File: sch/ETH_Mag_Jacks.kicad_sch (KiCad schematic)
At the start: 3 parts, among them J1 0826-1X4T-HS-F, J2 0826-1X4T-HS-F

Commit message: Project recovered
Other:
- company: (none) -> Karlsruhe Institute of Technology (KIT)
- title: (none) -> ATCA Simple Loopback HUB
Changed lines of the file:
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@@
 (kicad_sch (version 20230121) (generator eeschema)
   (paper "A4")
+  (title_block
+    (title "ATCA Simple Loopback HUB")
+    (date "2023-09-12")
+    (rev "1.0")
+    (company "Karlsruhe Institute of Technology (KIT)")
+    (comment 1 "Institute for Data Processing and Electronics (IPE)")
+    (comment 2 "Luis Ardila")
+    (comment 3 "IPE-380-06")
+    (comment 4 "Licensed under CERN-OHL-P-2.0")
+  )
   (no_connect (at 241.3 72.39))
   (no_connect (at 241.3 124.46))
@@
     (pin "9_4")
     (instances
-      (project "atca_simple_hub"
+      (project "atca-simple-loopback-hub"
         (path "/b1bf14e0-f6d2-45a7-b67f-6500a354b7ad/721cf5b7-470b-44a1-8f61-80b0cd462786"
           (reference "J1") (unit 1)
@@
     (pin "9_4")
     (instances
-      (project "atca_simple_hub"
+      (project "atca-simple-loopback-hub"
         (path "/b1bf14e0-f6d2-45a7-b67f-6500a354b7ad/721cf5b7-470b-44a1-8f61-80b0cd462786"
           (reference "J1") (unit 1)
@@
     (pin "9_4")
     (instances
-      (project "atca_simple_hub"
+      (project "atca-simple-loopback-hub"
         (path "/b1bf14e0-f6d2-45a7-b67f-6500a354b7ad/9c66bb85-f11b-42a4-b8f0-ea5e834ff554"
           (reference "J2") (unit 3)
@@
     (pin "9_4")
     (instances
-      (project "atca_simple_hub"
+      (project "atca-simple-loopback-hub"
         (path "/b1bf14e0-f6d2-45a7-b67f-6500a354b7ad/9c66bb85-f11b-42a4-b8f0-ea5e834ff554"
           (reference "J1") (unit 4)
@@
     (pin "9_4")
     (instances
-      (project "atca_simple_hub"
+      (project "atca-simple-loopback-hub"
         (path "/b1bf14e0-f6d2-45a7-b67f-6500a354b7ad/9c66bb85-f11b-42a4-b8f0-ea5e834ff554"
           (reference "J2") (unit 4)
@@
     (pin "9_4")
     (instances
-      (project "atca_simple_hub"
+      (project "atca-simple-loopback-hub"
         (path "/b1bf14e0-f6d2-45a7-b67f-6500a354b7ad/9c66bb85-f11b-42a4-b8f0-ea5e834ff554"
           (reference "J1") (unit 3)
@@
     (pin "9_4")
     (instances
-      (project "atca_simple_hub"
+      (project "atca-simple-loopback-hub"
         (path "/b1bf14e0-f6d2-45a7-b67f-6500a354b7ad/721cf5b7-470b-44a1-8f61-80b0cd462786"
           (reference "J1") (unit 2)
@@
     (pin "9_4")
     (instances
-      (project "atca_simple_hub"
+      (project "atca-simple-loopback-hub"
         (path "/b1bf14e0-f6d2-45a7-b67f-6500a354b7ad/721cf5b7-470b-44a1-8f61-80b0cd462786"
           (reference "J1") (unit 2)

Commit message: sch work
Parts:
- added C45 (x8), C47 (x8), C49 (x8), C59 (x8): 100nF, Capacitor_SMD:C_0402_1005Metric, symbol Device:C
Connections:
- net Z2_BI1.A_N: now also J1.10_1 (TRD1-_1)
- net Z2_BI1.A_P: now also J1.11_1 (TRD1+_1)
- net Z2_BI1.B_N: now also J1.5_1 (TRD2-_1)
- net Z2_BI1.B_P: now also J1.4_1 (TRD2+_1)
- net Z2_BI1.C_N: now also J1.2_1 (TRD3-_1)
- net Z2_BI1.C_P: now also J1.3_1 (TRD3+_1)
- net Z2_BI1.D_N: now also J1.9_1 (TRD4-_1)
- net Z2_BI1.D_P: now also J1.8_1 (TRD4+_1)
- net Z2_BI2.A_N: now also J1.10_2 (TRD1-_2)
- net Z2_BI2.A_P: now also J1.11_2 (TRD1+_2)
- net Z2_BI2.B_N: now also J1.5_2 (TRD2-_2)
- net Z2_BI2.B_P: now also J1.4_2 (TRD2+_2)
- net Z2_BI2.C_N: now also J1.2_2 (TRD3-_2)
- net Z2_BI2.C_P: now also J1.3_2 (TRD3+_2)
- net Z2_BI2.D_N: now also J1.9_2 (TRD4-_2)
- net Z2_BI2.D_P: now also J1.8_2 (TRD4+_2)
- net Z2_BI3.A_N: now also J1.10_4 (TRD1-_4)
- net Z2_BI3.A_P: now also J1.11_4 (TRD1+_4)
- net Z2_BI3.B_N: now also J1.5_4 (TRD2-_4)
- net Z2_BI3.B_P: now also J1.4_4 (TRD2+_4)
- net Z2_BI3.C_N: now also J1.2_4 (TRD3-_4)
- net Z2_BI3.C_P: now also J1.3_4 (TRD3+_4)
- net Z2_BI3.D_N: now also J1.9_4 (TRD4-_4)
- net Z2_BI3.D_P: now also J1.8_4 (TRD4+_4)
- net Z2_BI4.A_N: now also J1.10_3 (TRD1-_3)
- net Z2_BI4.A_P: now also J1.11_3 (TRD1+_3)
- net Z2_BI4.B_N: now also J1.5_3 (TRD2-_3)
- net Z2_BI4.B_P: now also J1.4_3 (TRD2+_3)
- net Z2_BI4.C_N: now also J1.2_3 (TRD3-_3)
- net Z2_BI4.C_P: now also J1.3_3 (TRD3+_3)
- net Z2_BI4.D_N: now also J1.9_3 (TRD4-_3)
- net Z2_BI4.D_P: now also J1.8_3 (TRD4+_3)
- net Z2_BI5.A_N: now also J1.10_1 (TRD1-_1)
- net Z2_BI5.A_P: now also J1.11_1 (TRD1+_1)
- net Z2_BI5.B_N: now also J1.5_1 (TRD2-_1)
- net Z2_BI5.B_P: now also J1.4_1 (TRD2+_1)
- net Z2_BI5.C_N: now also J1.2_1 (TRD3-_1)
- net Z2_BI5.C_P: now also J1.3_1 (TRD3+_1)
- net Z2_BI5.D_N: now also J1.9_1 (TRD4-_1)
- net Z2_BI5.D_P: now also J1.8_1 (TRD4+_1)
- net Z2_BI6.A_N: now also J1.10_2 (TRD1-_2)
- net Z2_BI6.A_P: now also J1.11_2 (TRD1+_2)
- net Z2_BI6.B_N: now also J1.5_2 (TRD2-_2)
- net Z2_BI6.B_P: now also J1.4_2 (TRD2+_2)
- net Z2_BI6.C_N: now also J1.2_2 (TRD3-_2)
- net Z2_BI6.C_P: now also J1.3_2 (TRD3+_2)
- net Z2_BI6.D_N: now also J1.9_2 (TRD4-_2)
- net Z2_BI6.D_P: now also J1.8_2 (TRD4+_2)
- net Z2_BI7.A_N: now also J2.10_4 (TRD1-_4)
- net Z2_BI7.A_P: now also J2.11_4 (TRD1+_4)
- net Z2_BI7.B_N: now also J2.5_4 (TRD2-_4)
- net Z2_BI7.B_P: now also J2.4_4 (TRD2+_4)
- net Z2_BI7.C_N: now also J2.2_4 (TRD3-_4)
- net Z2_BI7.C_P: now also J2.3_4 (TRD3+_4)
- net Z2_BI7.D_N: now also J2.9_4 (TRD4-_4)
- net Z2_BI7.D_P: now also J2.8_4 (TRD4+_4)
- net Z2_BI8.A_N: now also J2.10_3 (TRD1-_3)
- net Z2_BI8.A_P: now also J2.11_3 (TRD1+_3)
- net Z2_BI8.B_N: now also J2.5_3 (TRD2-_3)
- net Z2_BI8.B_P: now also J2.4_3 (TRD2+_3)
- net Z2_BI8.C_N: now also J2.2_3 (TRD3-_3)
- net Z2_BI8.C_P: now also J2.3_3 (TRD3+_3)
- net Z2_BI8.D_N: now also J2.9_3 (TRD4-_3)
- net Z2_BI8.D_P: now also J2.8_3 (TRD4+_3)
- net at J1.12_1 (TRCT1_1): now also C45.1 (x2)
- net at J1.1_1 (TRCT3_1): now also C49.1 (x2)
- net at J1.6_1 (TRCT2_1): now also C47.1 (x2)
- net at J1.7_1 (TRCT4_1): now also C59.1 (x2)
- net GNDPWR: now reaches J1.S1 (SHIELD), J1.S2 (SHIELD)
- net GNDPWR: now also J1.S1 (SHIELD), J1.S2 (SHIELD)
- net at J2.12_3 (TRCT1_3): now also C45.1
- net at J2.1_3 (TRCT3_3): now also C49.1
- net at J2.6_3 (TRCT2_3): now also C47.1
- net at J2.7_3 (TRCT4_3): now also C59.1
- net at J1.12_4 (TRCT1_4): now also C45.1
- net at J1.1_4 (TRCT3_4): now also C49.1
- net at J1.6_4 (TRCT2_4): now also C47.1
- net at J1.7_4 (TRCT4_4): now also C59.1
- net at J2.12_4 (TRCT1_4): now also C45.1
- net at J2.1_4 (TRCT3_4): now also C49.1
- net at J2.6_4 (TRCT2_4): now also C47.1
- net at J2.7_4 (TRCT4_4): now also C59.1
- net at J1.12_3 (TRCT1_3): now also C45.1
- net at J1.1_3 (TRCT3_3): now also C49.1
- net at J1.6_3 (TRCT2_3): now also C47.1
- net at J1.7_3 (TRCT4_3): now also C59.1
- net at J1.12_2 (TRCT1_2): now also C45.1 (x2)
- net at J1.1_2 (TRCT3_2): now also C49.1 (x2)
- net at J1.6_2 (TRCT2_2): now also C47.1 (x2)
- net at J1.7_2 (TRCT4_2): now also C59.1 (x2)
- new net GND: C45.2, C45.2, C45.2, C45.2, C45.2, C45.2, C45.2, C45.2, C47.2, C47.2, C47.2, C47.2, C47.2, C47.2, C47.2, C47.2, C49.2, C49.2, C49.2, C49.2, C49.2, C49.2, C49.2, C49.2, C59.2, C59.2, C59.2, C59.2, C59.2, C59.2, C59.2, C59.2
- no-connect marks 68 -> 64
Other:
- moved on the sheet: J1A, J1B, J1C, J1D

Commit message: before sch review
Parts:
- renumbered C59 to C100, C45 to C52, C47 to C53, C49 to C54, C59 to C55, C45 to C66, C47 to C67, C49 to C68, C59 to C69, C45 to C70, C47 to C71, C49 to C72, C59 to C73, C45 to C74, C47 to C75, C49 to C76, C59 to C83, C45 to C85, C47 to C86, C49 to C87, C59 to C88, C45 to C89, C47 to C90, C49 to C91, C59 to C92, C45 to C93, C47 to C94, C49 to C95, C59 to C96, C45 to C97, C47 to C98, C49 to C99

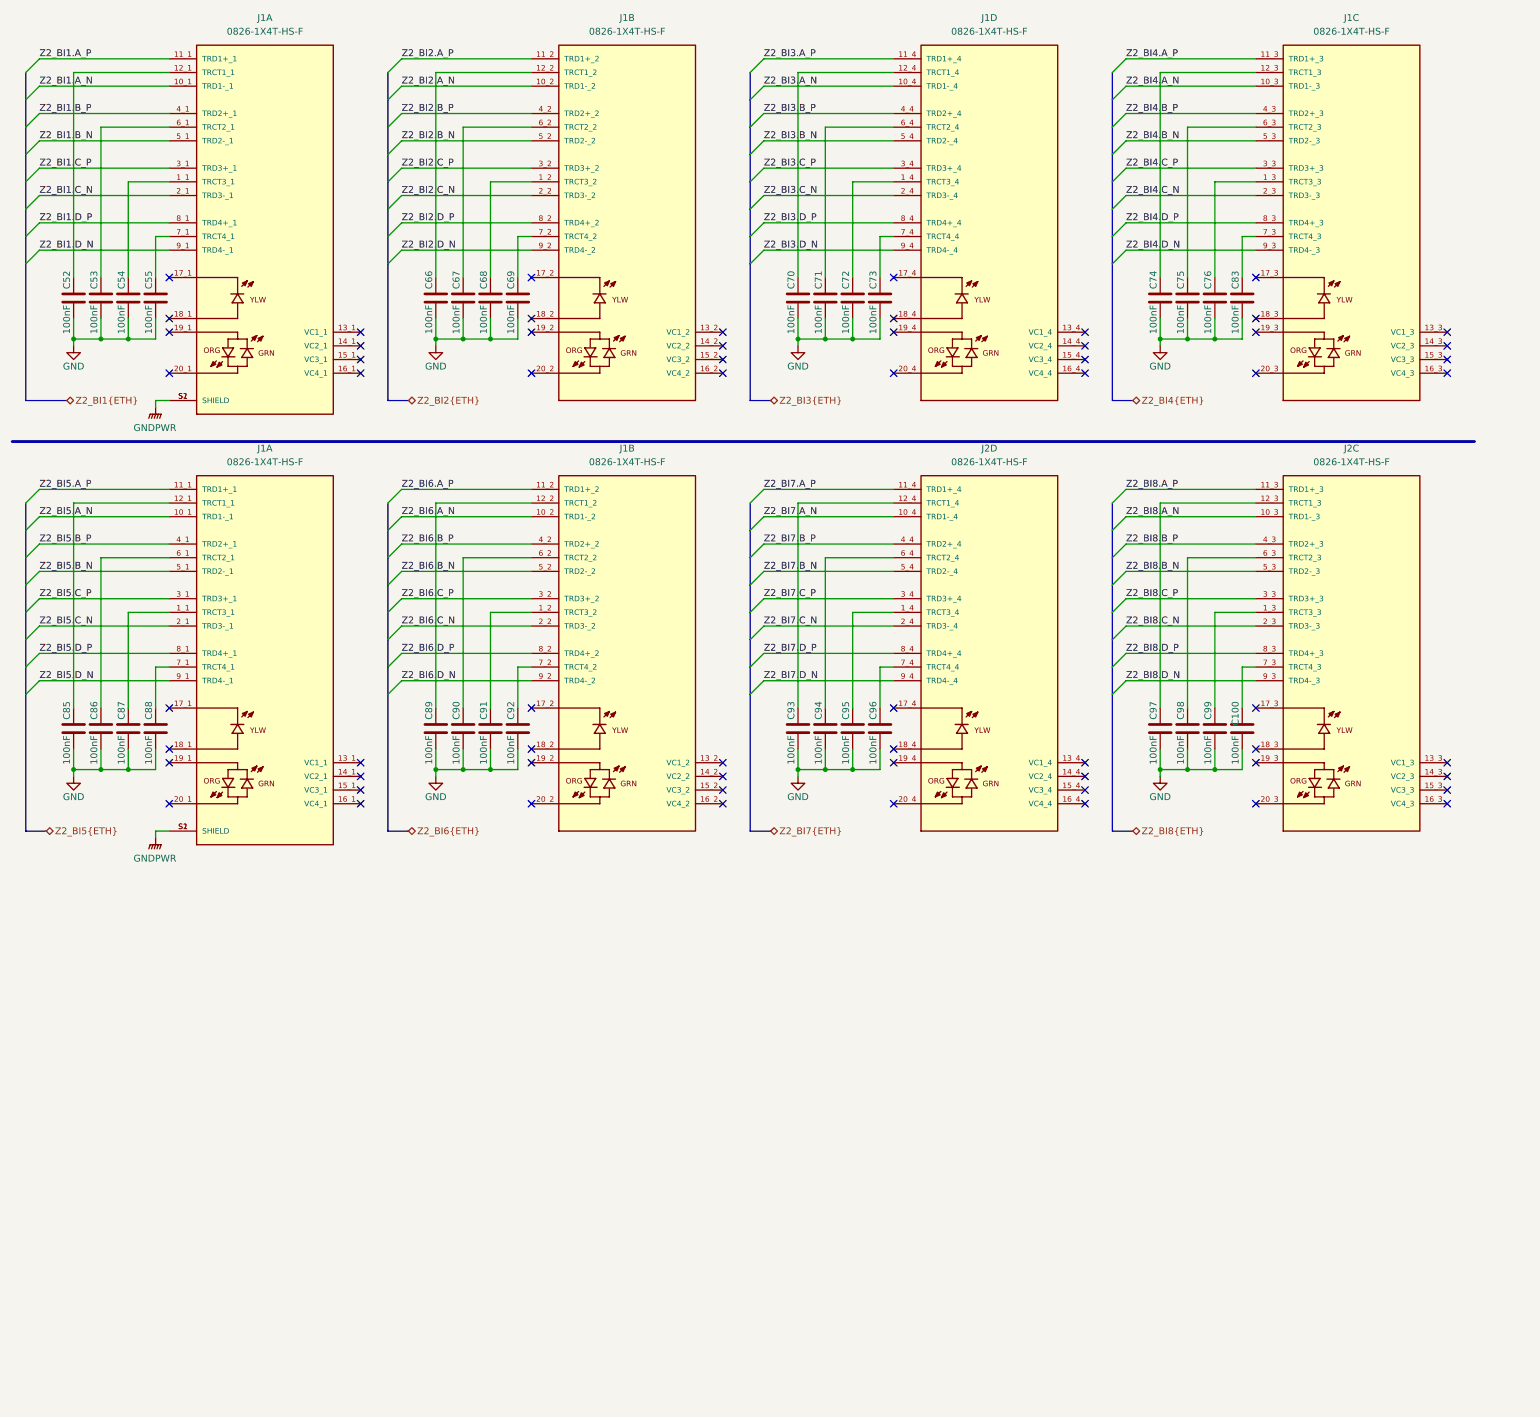
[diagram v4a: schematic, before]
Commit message: started changes from review
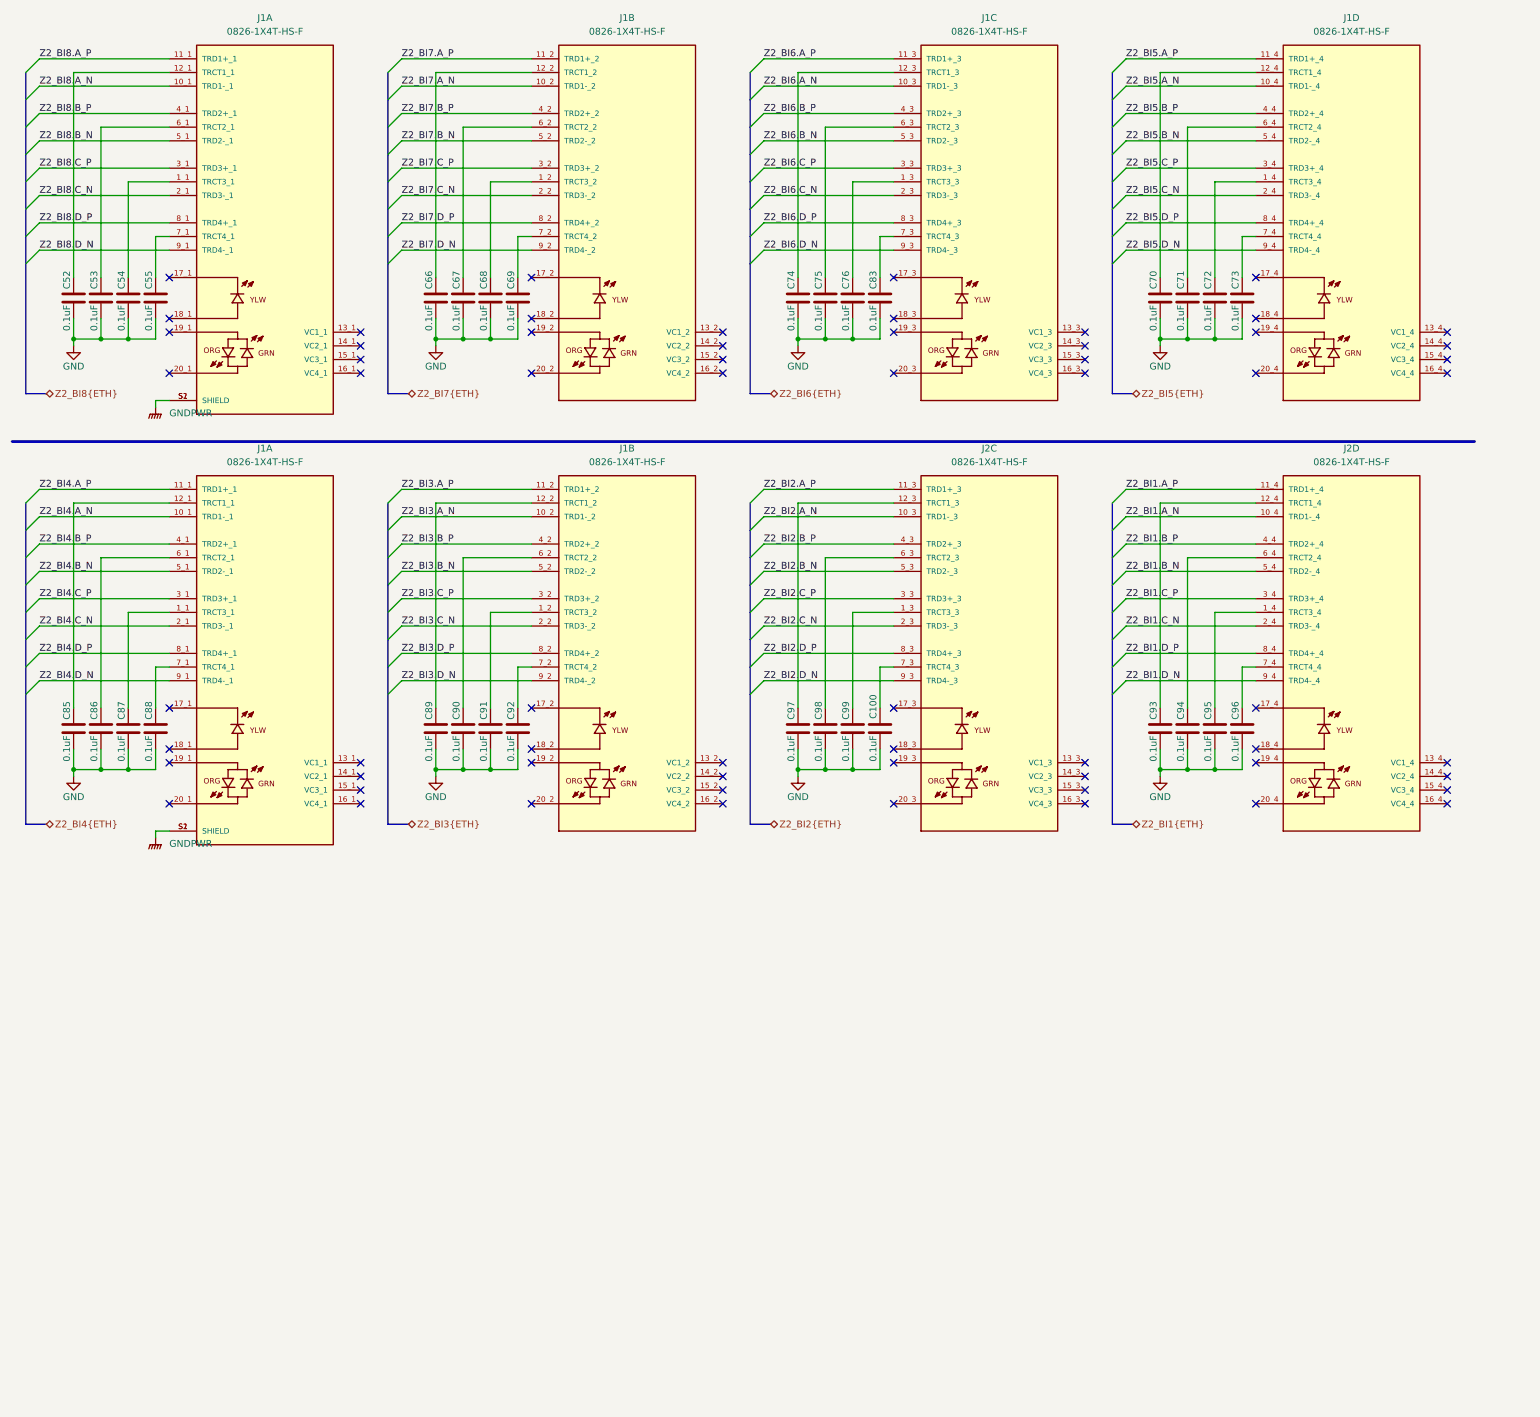
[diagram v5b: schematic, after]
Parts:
- C100, C52, C53, C54, C55, C66, C67, C68, C69, C70, C71, C72, C73, C74, C75, C76, C83, C85, C86, C87, C88, C89, C90, C91, C92, C93, C94, C95, C96, C97, C98, C99: value 100nF -> 0.1uF
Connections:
- net Z2_BI1.A_N: now also J2.10_4 (TRD1-_4); no longer J1.10_1 (TRD1-_1)
- net Z2_BI1.A_P: now also J2.11_4 (TRD1+_4); no longer J1.11_1 (TRD1+_1)
- net Z2_BI1.B_N: now also J2.5_4 (TRD2-_4); no longer J1.5_1 (TRD2-_1)
- net Z2_BI1.B_P: now also J2.4_4 (TRD2+_4); no longer J1.4_1 (TRD2+_1)
- net Z2_BI1.C_N: now also J2.2_4 (TRD3-_4); no longer J1.2_1 (TRD3-_1)
- net Z2_BI1.C_P: now also J2.3_4 (TRD3+_4); no longer J1.3_1 (TRD3+_1)
- net Z2_BI1.D_N: now also J2.9_4 (TRD4-_4); no longer J1.9_1 (TRD4-_1)
- net Z2_BI1.D_P: now also J2.8_4 (TRD4+_4); no longer J1.8_1 (TRD4+_1)
- net Z2_BI2.A_N: now also J2.10_3 (TRD1-_3); no longer J1.10_2 (TRD1-_2)
- net Z2_BI2.A_P: now also J2.11_3 (TRD1+_3); no longer J1.11_2 (TRD1+_2)
- net Z2_BI2.B_N: now also J2.5_3 (TRD2-_3); no longer J1.5_2 (TRD2-_2)
- net Z2_BI2.B_P: now also J2.4_3 (TRD2+_3); no longer J1.4_2 (TRD2+_2)
- net Z2_BI2.C_N: now also J2.2_3 (TRD3-_3); no longer J1.2_2 (TRD3-_2)
- net Z2_BI2.C_P: now also J2.3_3 (TRD3+_3); no longer J1.3_2 (TRD3+_2)
- net Z2_BI2.D_N: now also J2.9_3 (TRD4-_3); no longer J1.9_2 (TRD4-_2)
- net Z2_BI2.D_P: now also J2.8_3 (TRD4+_3); no longer J1.8_2 (TRD4+_2)
- net Z2_BI3.A_N: now also J1.10_2 (TRD1-_2); no longer J1.10_4 (TRD1-_4)
- net Z2_BI3.A_P: now also J1.11_2 (TRD1+_2); no longer J1.11_4 (TRD1+_4)
- net Z2_BI3.B_N: now also J1.5_2 (TRD2-_2); no longer J1.5_4 (TRD2-_4)
- net Z2_BI3.B_P: now also J1.4_2 (TRD2+_2); no longer J1.4_4 (TRD2+_4)
- net Z2_BI3.C_N: now also J1.2_2 (TRD3-_2); no longer J1.2_4 (TRD3-_4)
- net Z2_BI3.C_P: now also J1.3_2 (TRD3+_2); no longer J1.3_4 (TRD3+_4)
- net Z2_BI3.D_N: now also J1.9_2 (TRD4-_2); no longer J1.9_4 (TRD4-_4)
- net Z2_BI3.D_P: now also J1.8_2 (TRD4+_2); no longer J1.8_4 (TRD4+_4)
- net Z2_BI4.A_N: now also J1.10_1 (TRD1-_1); no longer J1.10_3 (TRD1-_3)
- net Z2_BI4.A_P: now also J1.11_1 (TRD1+_1); no longer J1.11_3 (TRD1+_3)
- net Z2_BI4.B_N: now also J1.5_1 (TRD2-_1); no longer J1.5_3 (TRD2-_3)
- net Z2_BI4.B_P: now also J1.4_1 (TRD2+_1); no longer J1.4_3 (TRD2+_3)
- net Z2_BI4.C_N: now also J1.2_1 (TRD3-_1); no longer J1.2_3 (TRD3-_3)
- net Z2_BI4.C_P: now also J1.3_1 (TRD3+_1); no longer J1.3_3 (TRD3+_3)
- net Z2_BI4.D_N: now also J1.9_1 (TRD4-_1); no longer J1.9_3 (TRD4-_3)
- net Z2_BI4.D_P: now also J1.8_1 (TRD4+_1); no longer J1.8_3 (TRD4+_3)
- net Z2_BI5.A_N: now also J1.10_4 (TRD1-_4); no longer J1.10_1 (TRD1-_1)
- net Z2_BI5.A_P: now also J1.11_4 (TRD1+_4); no longer J1.11_1 (TRD1+_1)
- net Z2_BI5.B_N: now also J1.5_4 (TRD2-_4); no longer J1.5_1 (TRD2-_1)
- net Z2_BI5.B_P: now also J1.4_4 (TRD2+_4); no longer J1.4_1 (TRD2+_1)
- net Z2_BI5.C_N: now also J1.2_4 (TRD3-_4); no longer J1.2_1 (TRD3-_1)
- net Z2_BI5.C_P: now also J1.3_4 (TRD3+_4); no longer J1.3_1 (TRD3+_1)
- net Z2_BI5.D_N: now also J1.9_4 (TRD4-_4); no longer J1.9_1 (TRD4-_1)
- net Z2_BI5.D_P: now also J1.8_4 (TRD4+_4); no longer J1.8_1 (TRD4+_1)
- net Z2_BI6.A_N: now also J1.10_3 (TRD1-_3); no longer J1.10_2 (TRD1-_2)
- net Z2_BI6.A_P: now also J1.11_3 (TRD1+_3); no longer J1.11_2 (TRD1+_2)
- net Z2_BI6.B_N: now also J1.5_3 (TRD2-_3); no longer J1.5_2 (TRD2-_2)
- net Z2_BI6.B_P: now also J1.4_3 (TRD2+_3); no longer J1.4_2 (TRD2+_2)
- net Z2_BI6.C_N: now also J1.2_3 (TRD3-_3); no longer J1.2_2 (TRD3-_2)
- net Z2_BI6.C_P: now also J1.3_3 (TRD3+_3); no longer J1.3_2 (TRD3+_2)
- net Z2_BI6.D_N: now also J1.9_3 (TRD4-_3); no longer J1.9_2 (TRD4-_2)
- net Z2_BI6.D_P: now also J1.8_3 (TRD4+_3); no longer J1.8_2 (TRD4+_2)
- net Z2_BI7.A_N: now also J1.10_2 (TRD1-_2); no longer J2.10_4 (TRD1-_4)
- net Z2_BI7.A_P: now also J1.11_2 (TRD1+_2); no longer J2.11_4 (TRD1+_4)
- net Z2_BI7.B_N: now also J1.5_2 (TRD2-_2); no longer J2.5_4 (TRD2-_4)
- net Z2_BI7.B_P: now also J1.4_2 (TRD2+_2); no longer J2.4_4 (TRD2+_4)
- net Z2_BI7.C_N: now also J1.2_2 (TRD3-_2); no longer J2.2_4 (TRD3-_4)
- net Z2_BI7.C_P: now also J1.3_2 (TRD3+_2); no longer J2.3_4 (TRD3+_4)
- net Z2_BI7.D_N: now also J1.9_2 (TRD4-_2); no longer J2.9_4 (TRD4-_4)
- net Z2_BI7.D_P: now also J1.8_2 (TRD4+_2); no longer J2.8_4 (TRD4+_4)
- net Z2_BI8.A_N: now also J1.10_1 (TRD1-_1); no longer J2.10_3 (TRD1-_3)
- net Z2_BI8.A_P: now also J1.11_1 (TRD1+_1); no longer J2.11_3 (TRD1+_3)
- net Z2_BI8.B_N: now also J1.5_1 (TRD2-_1); no longer J2.5_3 (TRD2-_3)
- net Z2_BI8.B_P: now also J1.4_1 (TRD2+_1); no longer J2.4_3 (TRD2+_3)
- net Z2_BI8.C_N: now also J1.2_1 (TRD3-_1); no longer J2.2_3 (TRD3-_3)
- net Z2_BI8.C_P: now also J1.3_1 (TRD3+_1); no longer J2.3_3 (TRD3+_3)
- net Z2_BI8.D_N: now also J1.9_1 (TRD4-_1); no longer J2.9_3 (TRD4-_3)
- net Z2_BI8.D_P: now also J1.8_1 (TRD4+_1); no longer J2.8_3 (TRD4+_3)
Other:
- moved on the sheet: C100, C70, C71, C72, C73, C74, C75, C76, C83, C93, C94, C95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

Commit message: update to v8
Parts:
- renumbered J1 to J2
